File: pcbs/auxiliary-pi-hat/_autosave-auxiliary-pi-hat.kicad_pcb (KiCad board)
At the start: 2 copper layers, 85 x 56 mm, 29 parts, among them J1 Conn_01x02, J10 Conn_01x03, J11 Conn_01x03, J2 Raspberry Pi - Hat Template -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, J3 Conn_01x03, J4 Conn_01x03, J5 Conn_01x03, J7 Conn_01x04, J8 Conn_02x04_Odd_Even, J9 Conn_01x05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

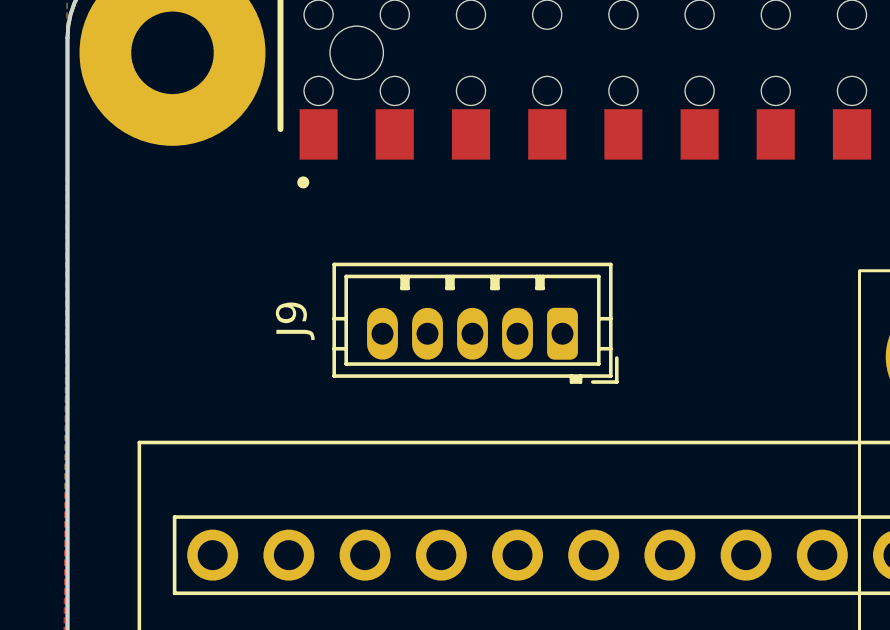
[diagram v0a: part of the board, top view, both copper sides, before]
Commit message: motor source upload; file reorg
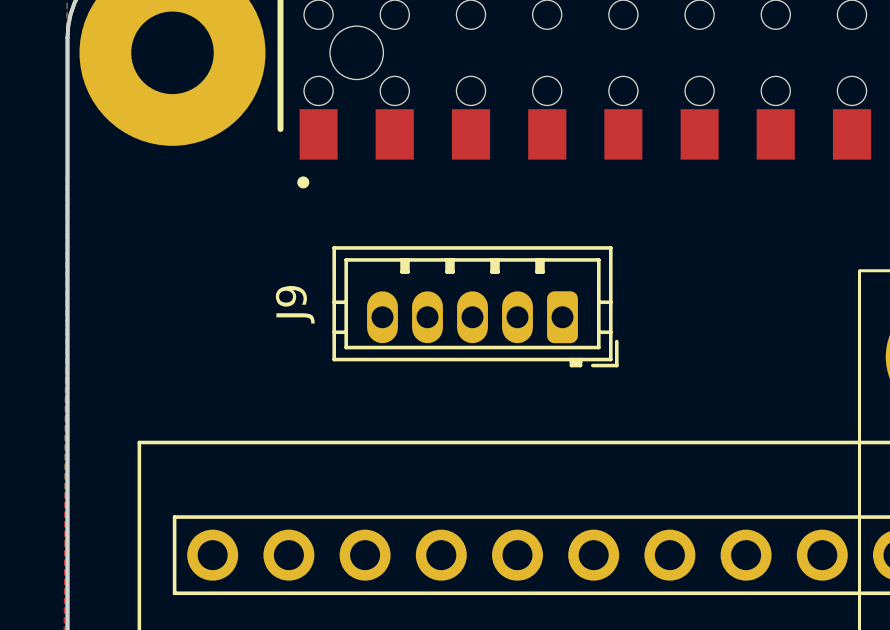
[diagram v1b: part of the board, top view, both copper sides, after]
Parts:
- moved J9 0.55 mm to (107.5, 59.5)
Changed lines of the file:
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@@
 	(footprint "Connector_JST:JST_ZH_B5B-ZR_1x05_P1.50mm_Vertical"
 		(layer "F.Cu")
-		(at 107.5 60 180)
+		(at 107.5 59.45 180)
 		(descr "JST ZH series connector, B5B-ZR (http://www.jst-mfg.com/product/pdf/eng/eZH.pdf), generated with kicad-footprint-generator")
 		(tags "connector JST ZH vertical")
